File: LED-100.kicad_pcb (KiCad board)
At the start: 2 copper layers, 97.8 x 97.8 mm, 99 parts, among them J2 LDA100_2_J2, J3 LDA100_2_J3, J4 LDA100_2_J4, J5 xtra, J6 Conn_01x09, J7 Conn_01x01, SW1 SW_SPDT, U1 TLC5947DAP, U2 TLC5947DAP, U3 TLC5947DAP

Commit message: pcb tweaks
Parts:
- LED TEST +5V: renamed from SW1
- moved TP2 108.0 mm to (154.3, 94.6)
- moved TP1 100.6 mm to (149.2, 94.6)
- moved C3 88.7 mm to (172.5, 92.3)
- moved J7 88.7 mm to (176.3, 79.6)
- moved R3 88.7 mm to (170.0, 89.8)
- moved U3 88.7 mm to (182.1, 95.6)
- moved D36 87.8 mm to (193.6, 71.0)
- moved D37 87.8 mm to (193.6, 78.6)
- moved D38 87.8 mm to (193.6, 73.6)
- moved D39a1 87.8 mm to (193.6, 76.1)
- moved D41 87.8 mm to (193.6, 86.2)
- moved D48 87.8 mm to (193.6, 96.4)
- moved D49 87.8 mm to (193.6, 93.9)
- moved D51 87.8 mm to (193.6, 99.0)
- moved J3 87.8 mm to (197.5, 134.5)
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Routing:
- net /SDA_B: track 74.8 -> 96.8 mm
- net /LATCH: track 130.7 -> 141.6 mm, vias 4 -> 5
- net /FADEOUT: track 23.5 -> 13.1 mm
- net +5V: track 167.6 -> 176.5 mm, vias 1 -> 2
- net /BLANK: track 155.5 -> 163.8 mm
- net /SDA_A: track 81.6 -> 89.9 mm
- net /SCL: track 117.8 -> 124.7 mm, vias 3 -> 4
- net /TEST5V: track 267.4 -> 273.1 mm
- net /SDA_C: track 37.9 -> 41.8 mm
- net Net-(J6-Pin_9): track 11.4 -> 8.25 mm
- net Net-(J6-Pin_8): track 11.4 -> 8.25 mm
- net Net-(J6-Pin_7): track 11.4 -> 8.25 mm
- net Net-(J6-Pin_6): track 11.4 -> 8.25 mm
- net Net-(J6-Pin_5): track 11.4 -> 8.25 mm
- net Net-(J6-Pin_1): track 11.4 -> 8.25 mm
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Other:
- board size 97.8 x 97.8 mm -> 100 x 100 mm
- board text added: "ON"
- board text removed: "Q46"

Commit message: cleanup
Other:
- board text added: "GO"
- board text removed: "ON"
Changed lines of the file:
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@@
     (effects (font (size 1 1) (thickness 0.1)) (justify left bottom))
   )
-  (gr_text "ON" (at 118.11 137.16) (layer "F.SilkS")
+  (gr_text "GO" (at 118.11 137.16) (layer "F.SilkS")
     (effects (font (size 0.8 0.8) (thickness 0.1)) (justify left bottom))
   )
@@
     (effects (font (size 0.8 0.8) (thickness 0.1)) (justify left bottom))
   )
-  (gr_text "Curr. Set" (at 169.693 87.884) (layer "F.SilkS")
+  (gr_text "Curr. Set" (at 169.545 88.265) (layer "F.SilkS")
     (effects (font (size 0.8 0.8) (thickness 0.1)) (justify left bottom))
   )
@@
     (effects (font (size 0.8 0.8) (thickness 0.1)) (justify left bottom))
   )
-  (gr_text "Curr. Set" (at 144.145 80.033 90) (layer "F.SilkS")
-    (effects (font (size 0.8 0.8) (thickness 0.1)) (justify left bottom))
-  )
+  (gr_text "Curr. Set" (at 144.145 79.375 90) (layer "F.SilkS")
+    (effects (font (size 0.8 0.8) (thickness 0.1)) (justify left bottom))
+  )

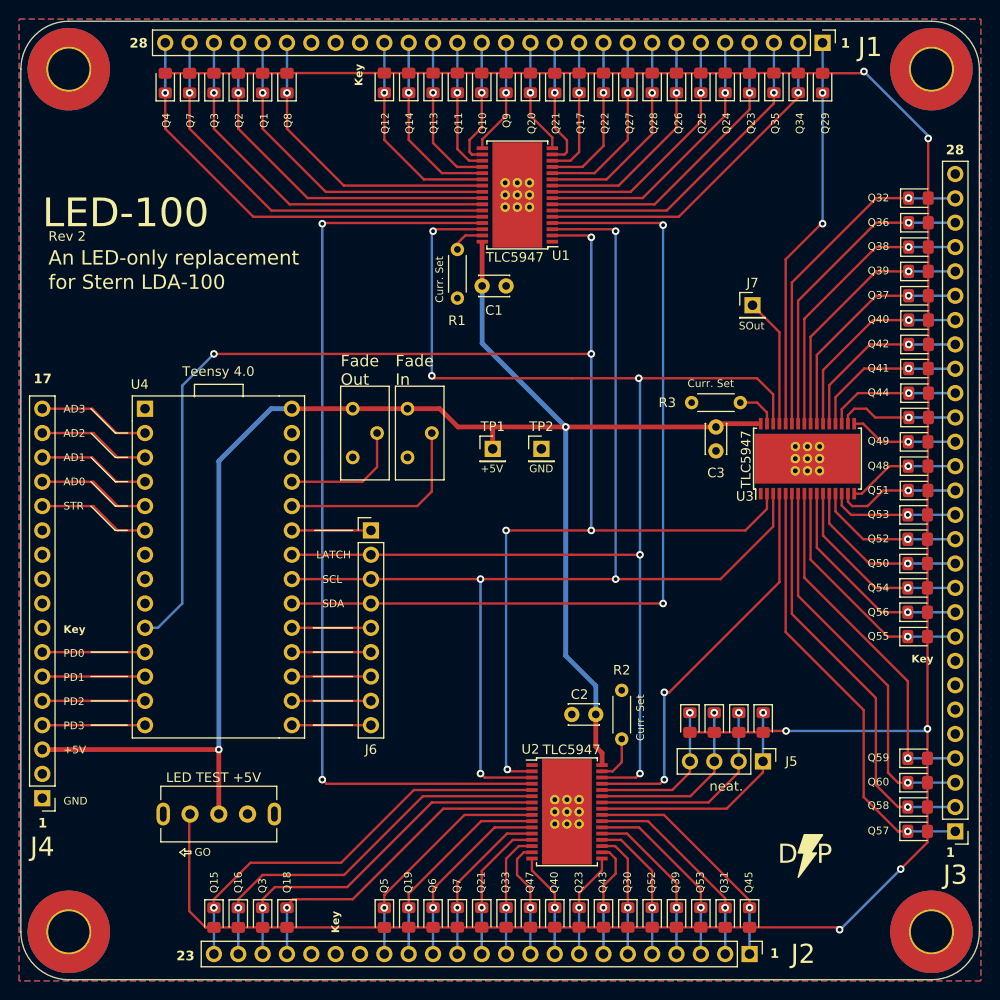
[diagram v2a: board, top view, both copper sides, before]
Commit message: use SPI instead of I2C
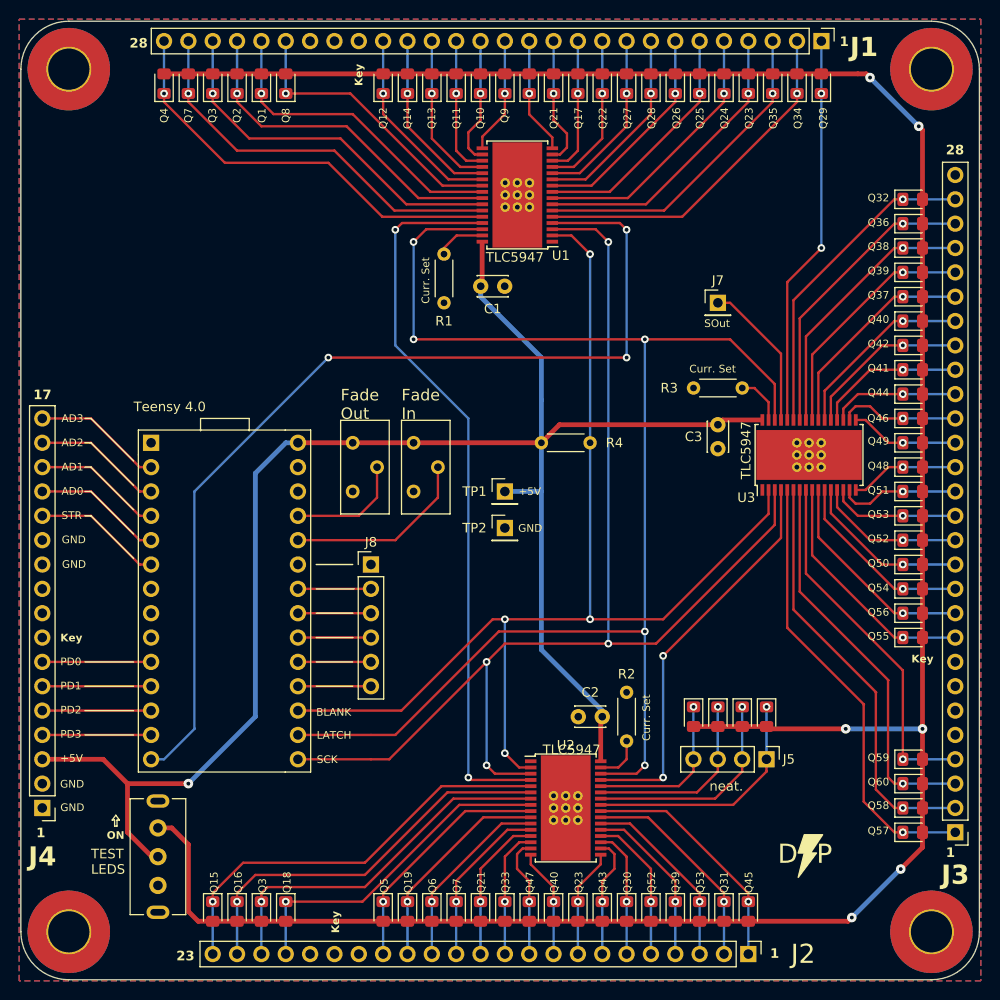
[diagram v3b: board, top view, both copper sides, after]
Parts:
- removed J6: Conn_01x09, Connector_PinHeader_2.54mm:PinHeader_1x09_P2.54mm_Vertical
- removed LED TEST +5V: SW_SPDT, Button_Switch_THT:SW_Slide_SPDT_SLW-12689-4A-N-D
- added J8: Conn_01x06, Connector_PinHeader_2.54mm:PinHeader_1x06_P2.54mm_Vertical, F.Cu at (136.5, 106.7)
- added R4: 100k, Resistor_THT:R_Axial_DIN0204_L3.6mm_D1.6mm_P5.08mm_Horizontal, F.Cu at (154.3, 94.0)
- added SW1: SW_SPDT, Button_Switch_THT:SW_Slide_SPDT_SLW-12689-4A-N-D, F.Cu at (114.3, 137.2)
- U4: value ~ -> TEENSY 4.0
- moved TP2 9.09 mm to (150.5, 102.9)
- moved R3 5.50 mm to (175.3, 88.3), turned to 180 degrees
- moved R2 5.31 mm to (163.2, 125.1), turned to 90 degrees
- moved R1 4.80 mm to (144.1, 74.3), turned to -90 degrees
- moved TP1 4.62 mm to (150.5, 99.1)
- moved J7 3.62 mm to (172.7, 79.4)
- moved U4 3.61 mm to (121.3, 109.2)
- moved RV1 3.61 mm to (141.0, 94.0)
- moved RV2 3.56 mm to (134.6, 94.0)
- moved J4 1.02 mm to (102.2, 132.1)
- moved D71 0.72 mm to (172.7, 122.6)
- moved D72 0.72 mm to (170.2, 122.6)
- moved C2 0.71 mm to (160.7, 122.6)
- moved D69 0.71 mm to (177.8, 122.6)
- moved D70 0.71 mm to (175.3, 122.6)
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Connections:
- net /SDA_B renamed /MISO_B
- net /SDA_C renamed /MISO_C
- R1 pad 1: GND -> Net-(U1-IREF)
- R1 pad 2: Net-(U1-IREF) -> GND
- R2 pad 1: GND -> Net-(U2-IREF)
- R2 pad 2: Net-(U2-IREF) -> GND
- R3 pad 1: GND -> Net-(U3-IREF)
- R3 pad 2: Net-(U3-IREF) -> GND
- U1 pad 3: /SCL -> /SCK
- U1 pad 30: /LATCH -> /LAT
- U1 pad 4: /SDA_A -> /MISO_A
- U2 pad 3: /SCL -> /SCK
- U2 pad 30: /LATCH -> /LAT
- U3 pad 3: /SCL -> /SCK
- U3 pad 30: /LATCH -> /LAT
- U4 pad 10: /BLANK -> Net-(J4-PD0)
- U4 pad 11: Net-(J4-PD0) -> Net-(J4-PD1)
- U4 pad 12: Net-(J4-PD1) -> Net-(J4-PD2)
- U4 pad 13: Net-(J4-PD2) -> Net-(J4-PD3)
- U4 pad 14: Net-(J4-PD3) -> /MISO_A
- U4 pad 15: Net-(J6-Pin_9) -> /SCK
- U4 pad 16: Net-(J6-Pin_8) -> /LAT
- U4 pad 17: Net-(J6-Pin_7) -> /BLANK
- U4 pad 20: /SDA_A -> Net-(J8-Pin_4)
- U4 pad 21: /SCL -> Net-(J8-Pin_3)
- U4 pad 22: /LATCH -> Net-(J8-Pin_2)
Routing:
- net /LAT: track 0.00 -> 151.9 mm, vias 0 -> 5
- net /LATCH: track 141.6 -> 0.00 mm, vias 5 -> 0
- net /SCK: track 0.00 -> 128.1 mm, vias 0 -> 4
- net /SCL: track 124.7 -> 0.00 mm, vias 4 -> 0
- net /MISO_A: track 0.00 -> 102.9 mm, vias 0 -> 3
- net /SDA_A: track 89.9 -> 0.00 mm, vias 2 -> 0
- net /BLANK: track 163.8 -> 120.8 mm, vias 6 -> 4
- net /MISO_B: track 96.8 -> 76.3 mm
- net Net-(J8-Pin_1): track 8.25 -> 0.00 mm
- net Net-(J6-Pin_9): track 8.25 -> 0.00 mm
- net Net-(J6-Pin_8): track 8.25 -> 0.00 mm
- net Net-(J6-Pin_7): track 8.25 -> 0.00 mm
- net Net-(J8-Pin_4): track 0.00 -> 8.18 mm
- net Net-(J8-Pin_3): track 0.00 -> 8.18 mm
- net Net-(J8-Pin_2): track 0.00 -> 8.18 mm
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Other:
- board text added: "BLANK"
- board text added: "ON"
- board text added: "Q46"
- board text added: "SCK"
- board text added: "TEST LEDS"
- board text removed: "An LED-only replacement"
- board text removed: "GO"
- board text removed: "LED-100"
- board text removed: "Q20"
- board text removed: "Rev 2"
- board text removed: "SCL"
- board text removed: "SDA"
- board text removed: "for Stern LDA-100"

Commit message: tweaks & cleanup
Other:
- board text added: "An ~e~n~s~m~o~o~t~h~e~n~e~d~ LED-only replacement for LDA-100"
- board text added: "Dynamic Intensity Lamp Driver Option"
- board text added: "IN SPEED"
- board text added: "LED-100"
- board text added: "OUT SPEED"
- board text removed: "Fade In"
- board text removed: "Fade Out"
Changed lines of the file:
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@@
     (thickness 1.6)
   )
-  (paper "A4")
+  (paper "USLetter")
+  (title_block
+    (title "LED-100")
+    (date "2025-03-19")
+    (rev "2")
+    (company "Duhan Power!")
+  )
   (layers
     (0 "F.Cu" signal)
@@
     (property "ki_keywords" "connector")
     (attr through_hole)
-    (fp_text reference "J8" (at 0 -2.33) (layer "F.SilkS")
+    (fp_text reference "J8" (at 2.667 0) (layer "F.SilkS")
         (effects (font (size 1 1) (thickness 0.15)))
     )
@@
     (effects (font (size 0.8 0.8) (thickness 0.1)) (justify left bottom))
   )
-  (gr_text "Fade\nIn" (at 139.71 91.635) (layer "F.SilkS")
+  (gr_text "IN\nSPEED" (at 139.411315 91.41832) (layer "F.SilkS")
     (effects (font (size 1.2 1.2) (thickness 0.15)) (justify left bottom))
   )
@@
     (effects (font (size 0.8 0.8) (thickness 0.1)) (justify left bottom))
   )
+  (gr_text "Dynamic Intensity Lamp Driver Option" (at 108.712 84.328 45) (layer "F.SilkS")
+    (effects (font (size 1 1) (thickness 0.15)) (justify left bottom))
+  )
   (gr_text "Q22" (at 161.18283 61.247896 90) (layer "F.SilkS")
     (effects (font (size 0.8 0.8) (thickness 0.1)) (justify left bottom))
@@
     (effects (font (size 0.8 0.8) (thickness 0.1)) (justify left bottom))
   )
+  (gr_text "An ~e~n~s~m~o~o~t~h~e~n~e~d~\nLED-only replacement for LDA-100" (at 111.76 87.376 45) (layer "F.SilkS")
+    (effects (font (size 1 1) (thickness 0.15)) (justify left bottom))
+  )
   (gr_text "Q3" (at 120.450597 60.612896 90) (layer "F.SilkS")
     (effects (font (size 0.8 0.8) (thickness 0.1)) (justify left bottom))
@@
     (effects (font (size 0.8 0.8) (thickness 0.1)) (justify left bottom))
   )
+  (gr_text "LED-100" (at 107.188 83.312 45) (layer "F.SilkS")
+    (effects (font (size 3 3) (thickness 0.3)) (justify left bottom))
+  )
   (gr_text "Curr. Set" (at 169.737985 86.739399) (layer "F.SilkS")
     (effects (font (size 0.8 0.8) (thickness 0.1)) (justify left bottom))
@@
     (effects (font (size 0.8 0.8) (thickness 0.1)) (justify left bottom))
   )
-  (gr_text "Fade\nOut" (at 133.36 91.635) (layer "F.SilkS")
+  (gr_text "OUT\nSPEED" (at 133.061315 91.41832) (layer "F.SilkS")
     (effects (font (size 1.2 1.2) (thickness 0.15)) (justify left bottom))
   )

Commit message: rev3 first draft
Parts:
- removed RV2: R_Potentiometer_US, Potentiometer_THT:Potentiometer_Bourns_3296Y_Vertical
- added BLANK: Conn_01x01, Connector_PinHeader_2.54mm:PinHeader_1x01_P2.54mm_Vertical, F.Cu at (167.6, 107.3)
- added LATCH: Conn_01x01, Connector_PinHeader_2.54mm:PinHeader_1x01_P2.54mm_Vertical, F.Cu at (167.6, 102.2)
- J8: footprint Connector_PinHeader_2.54mm:PinHeader_1x06_P2.54mm_Vertical -> Connector_PinHeader_2.54mm:PinHeader_1x07_P2.54mm_Vertical
- RV1: footprint Potentiometer_THT:Potentiometer_Bourns_3296Y_Vertical -> Potentiometer_THT:Potentiometer_Piher_PT-10-V10_Vertical
- moved TP2 9.47 mm to (156.7, 110.0)
- moved RV1 9.37 mm to (150.3, 94.1), turned to 180 degrees
- moved TP1 8.55 mm to (156.7, 104.9)
- moved SW1 7.96 mm to (121.3, 133.3), turned to 0 degrees
- moved REF** 2.62 mm to (182.2, 136.5)
- moved J8 2.55 mm to (136.5, 104.1)
- moved C3 0.61 mm to (172.7, 91.5)
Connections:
- RV1 pad 2: /FADEIN -> /FADESPEED
- U4 pad 18: Net-(J8-Pin_6) -> Net-(J8-Pin_7)
- U4 pad 19: Net-(J8-Pin_5) -> Net-(J8-Pin_6)
- U4 pad 20: Net-(J8-Pin_4) -> Net-(J8-Pin_5)
- U4 pad 21: Net-(J8-Pin_3) -> Net-(J8-Pin_4)
- U4 pad 22: Net-(J8-Pin_2) -> Net-(J8-Pin_3)
- U4 pad 23: Net-(J8-Pin_1) -> Net-(J8-Pin_2)
- U4 pad 24: /FADEIN -> Net-(J8-Pin_1)
- U4 pad 25: /FADEOUT -> /FADESPEED
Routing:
- net /FADEIN: track 20.2 -> 0.00 mm
- net /FADESPEED: track 0.00 -> 13.5 mm
- net /FADEOUT: track 12.8 -> 0.00 mm
- net /BLANK: track 120.8 -> 133.3 mm
- net Net-(J8-Pin_7): track 0.00 -> 8.18 mm
- net Net-(J8-Pin_1): track 0.00 -> 7.62 mm
- net +5V: track 178.9 -> 175.7 mm
- net /LAT: track 151.9 -> 154.1 mm
- net /TEST5V: track 271.5 -> 269.4 mm
- net /SCK: track 128.1 -> 126.5 mm
- net /MISO_A: track 102.9 -> 103.6 mm
- net Net-(J8-Pin_2): track 8.18 -> 7.62 mm
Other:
- board text added: "0"
- board text added: "10"
- board text added: "11"
- board text added: "12"
- board text added: "13"
- board text added: "14"
- board text added: "15"
- board text added: "16"
- board text added: "18"
- board text added: "19"
- board text added: "2"
- board text added: "20"
- board text added: "21"
- board text added: "22"
- board text added: "24"
- board text added: "3"
- board text added: "4"
- board text added: "5"
- board text added: "6"
- board text added: "7"
- board text added: "8"
- board text added: "9"
- board text added: "Dynamic Intensity LED Driver Output"
- board text added: "MISO"
- board text added: "OFF TO RUN"
- board text added: "ON TO DEBUG"
- board text added: "Rev. 3"
- board text added: "s~m~o~o~t~h"
- board text removed: "Dynamic Intensity Lamp Driver Option"
- board text removed: "IN SPEED"
- board text removed: "OUT SPEED"
- board text removed: "TEST LEDS"
